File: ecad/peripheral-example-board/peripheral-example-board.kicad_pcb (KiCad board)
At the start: 2 copper layers, 105 x 70 mm, 4 parts, among them J1 Amphenol_10061913-xx0, J2 Amphenol_ACJS-MHOM, J3 Amphenol_ACJS-MHOM, J4 PJRAS2X1S01AUX

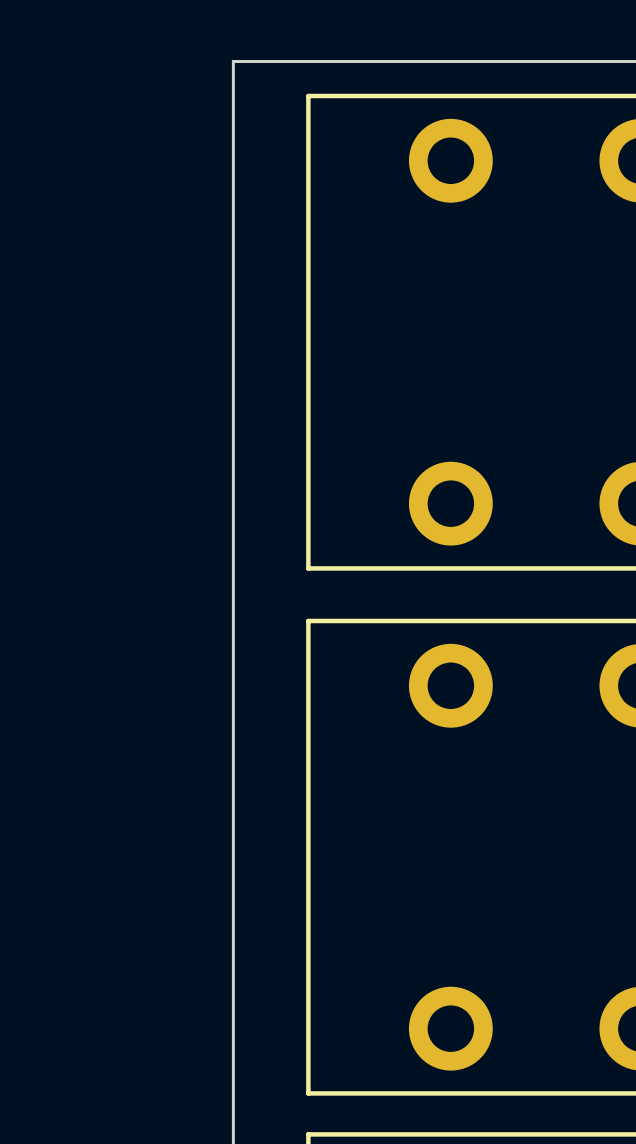
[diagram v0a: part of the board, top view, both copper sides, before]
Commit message: Good state for mechanical assembly, can bounce back to pcb review now that board outlines are close.
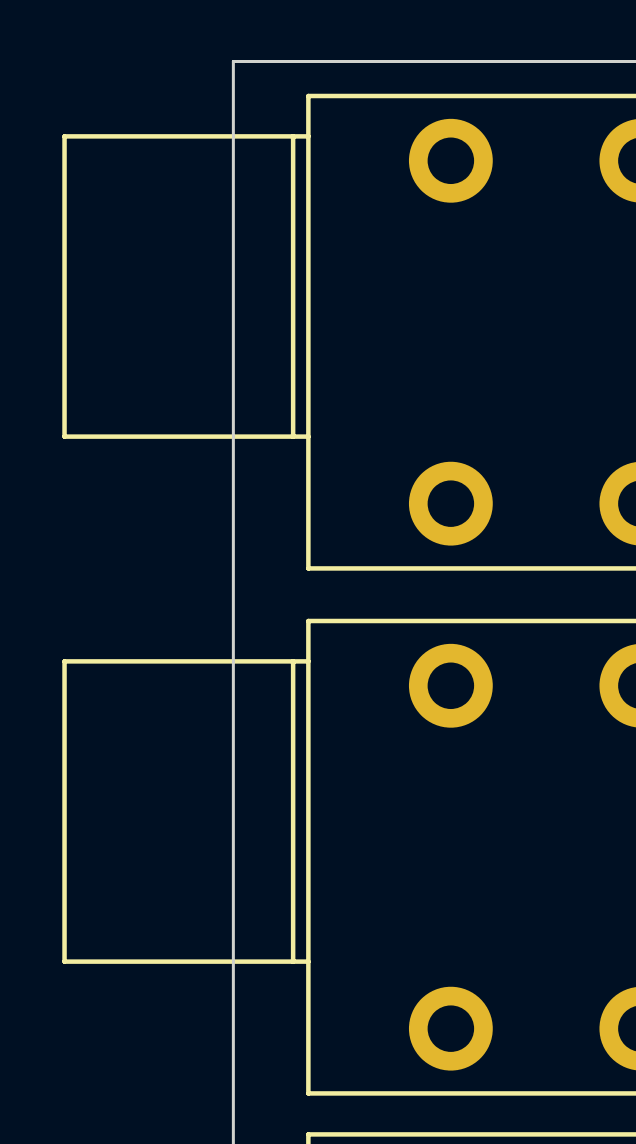
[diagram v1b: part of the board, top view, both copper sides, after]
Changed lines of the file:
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@@
     (fp_line (start 0 -9.398) (end 0 6.35)
       (stroke (width 0.15) (type solid)) (layer "F.SilkS"))
+    (fp_line (start 0 -5.0038) (end 8.128 -5.0038)
+      (stroke (width 0.15) (type solid)) (layer "F.SilkS"))
+    (fp_line (start 0 5.0038) (end 8.128 5.0038)
+      (stroke (width 0.15) (type solid)) (layer "F.SilkS"))
     (fp_line (start 0 6.35) (end -25.4 6.35)
       (stroke (width 0.15) (type solid)) (layer "F.SilkS"))
-    (fp_line (start 0 -5.0038) (end 8.128 -5.0038)
-      (stroke (width 0.15) (type solid)) (layer "Dwgs.User"))
-    (fp_line (start 0 5.0038) (end 8.128 5.0038)
-      (stroke (width 0.15) (type solid)) (layer "Dwgs.User"))
     (fp_line (start 0.508 -5.0038) (end 0.508 5.0038)
-      (stroke (width 0.15) (type solid)) (layer "Dwgs.User"))
+      (stroke (width 0.15) (type solid)) (layer "F.SilkS"))
     (fp_line (start 8.128 -5.0038) (end 8.128 5.0038)
-      (stroke (width 0.15) (type solid)) (layer "Dwgs.User"))
+      (stroke (width 0.15) (type solid)) (layer "F.SilkS"))
     (fp_line (start -25.654 -9.652) (end -25.654 6.604)
       (stroke (width 0.12) (type solid)) (layer "F.CrtYd"))
@@
     (fp_line (start 0 -9.398) (end 0 6.35)
       (stroke (width 0.15) (type solid)) (layer "F.SilkS"))
+    (fp_line (start 0 -5.0038) (end 8.128 -5.0038)
+      (stroke (width 0.15) (type solid)) (layer "F.SilkS"))
+    (fp_line (start 0 5.0038) (end 8.128 5.0038)
+      (stroke (width 0.15) (type solid)) (layer "F.SilkS"))
     (fp_line (start 0 6.35) (end -25.4 6.35)
       (stroke (width 0.15) (type solid)) (layer "F.SilkS"))
-    (fp_line (start 0 -5.0038) (end 8.128 -5.0038)
-      (stroke (width 0.15) (type solid)) (layer "Dwgs.User"))
-    (fp_line (start 0 5.0038) (end 8.128 5.0038)
-      (stroke (width 0.15) (type solid)) (layer "Dwgs.User"))
     (fp_line (start 0.508 -5.0038) (end 0.508 5.0038)
-      (stroke (width 0.15) (type solid)) (layer "Dwgs.User"))
+      (stroke (width 0.15) (type solid)) (layer "F.SilkS"))
     (fp_line (start 8.128 -5.0038) (end 8.128 5.0038)
-      (stroke (width 0.15) (type solid)) (layer "Dwgs.User"))
+      (stroke (width 0.15) (type solid)) (layer "F.SilkS"))
     (fp_line (start -25.654 -9.652) (end -25.654 6.604)
       (stroke (width 0.12) (type solid)) (layer "F.CrtYd"))
@@
     (style (thickness 0.15) (arrow_length 1.27) (text_position_mode 0) (extension_height 0.58642) (extension_offset 0.5) keep_text_aligned)
   )
+  (dimension (type aligned) (layer "Edge.Cuts")
+    (pts (xy 97.5 70.5) (xy 202.5 70.5))
+    (height -4.25)
+    (gr_text "105.0000 mm" (at 150 65.1) (layer "Edge.Cuts")
+      (effects (font (size 1 1) (thickness 0.15)))
+    )
+    (format (prefix "") (suffix "") (units 3) (units_format 1) (precision 4))
+    (style (thickness 0.1) (arrow_length 1.27) (text_position_mode 0) (extension_height 0.58642) (extension_offset 0.5) keep_text_aligned)
+  )
+  (dimension (type aligned) (layer "Edge.Cuts")
+    (pts (xy 202.5 70.5) (xy 202.5 140.5))
+    (height -5)
+    (gr_text "70.0000 mm" (at 206.35 105.5 90) (layer "Edge.Cuts")
+      (effects (font (size 1 1) (thickness 0.15)))
+    )
+    (format (prefix "") (suffix "") (units 3) (units_format 1) (precision 4))
+    (style (thickness 0.1) (arrow_length 1.27) (text_position_mode 0) (extension_height 0.58642) (extension_offset 0.5) keep_text_aligned)
+  )
+  (dimension (type aligned) (layer "Edge.Cuts")
+    (pts (xy 97.5 70.5) (xy 162.75 70.5))
+    (height -1.75)
+    (gr_text "65.2500 mm" (at 130.125 67.6) (layer "Edge.Cuts")
+      (effects (font (size 1 1) (thickness 0.15)))
+    )
+    (format (prefix "") (suffix "") (units 3) (units_format 1) (precision 4))
+    (style (thickness 0.1) (arrow_length 1.27) (text_position_mode 0) (extension_height 0.58642) (extension_offset 0.5) keep_text_aligned)
+  )
 )

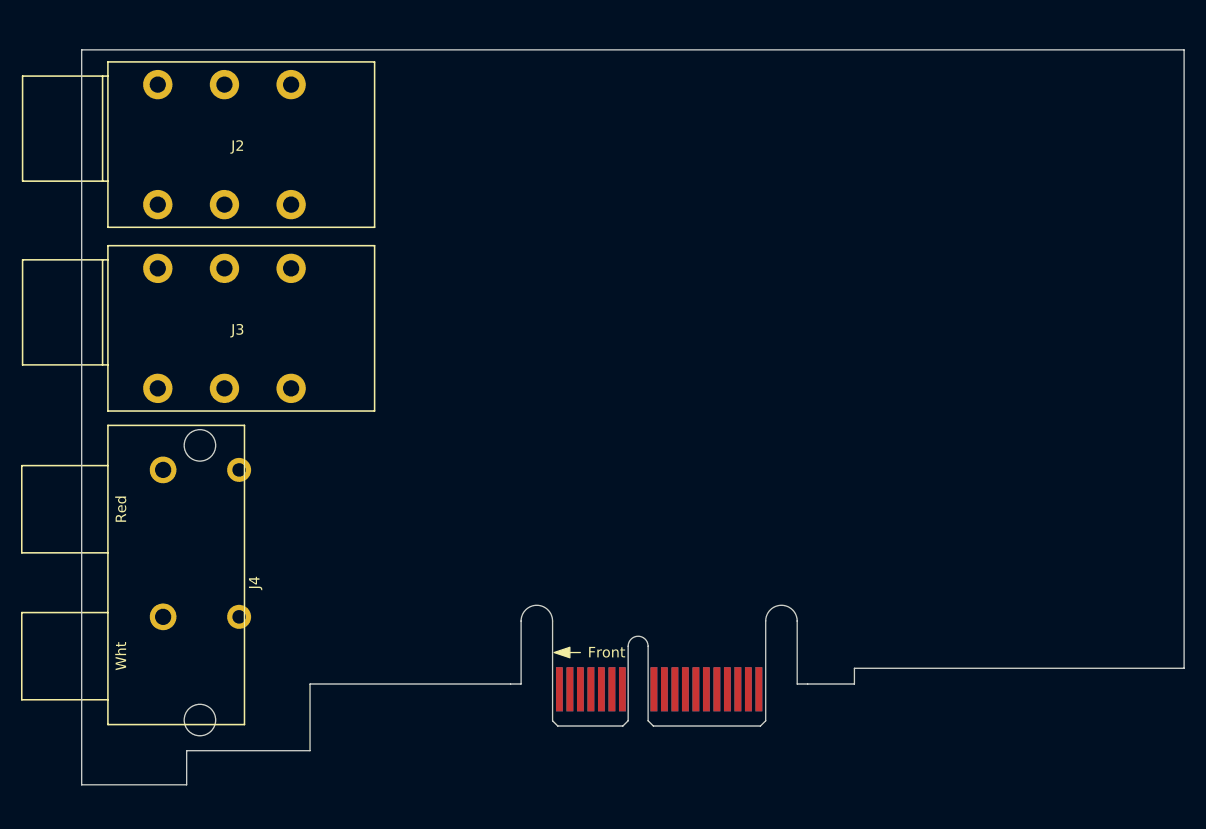
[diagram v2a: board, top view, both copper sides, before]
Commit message: Version 0.1 of the peripheral example board sent to PCB manufaturer.
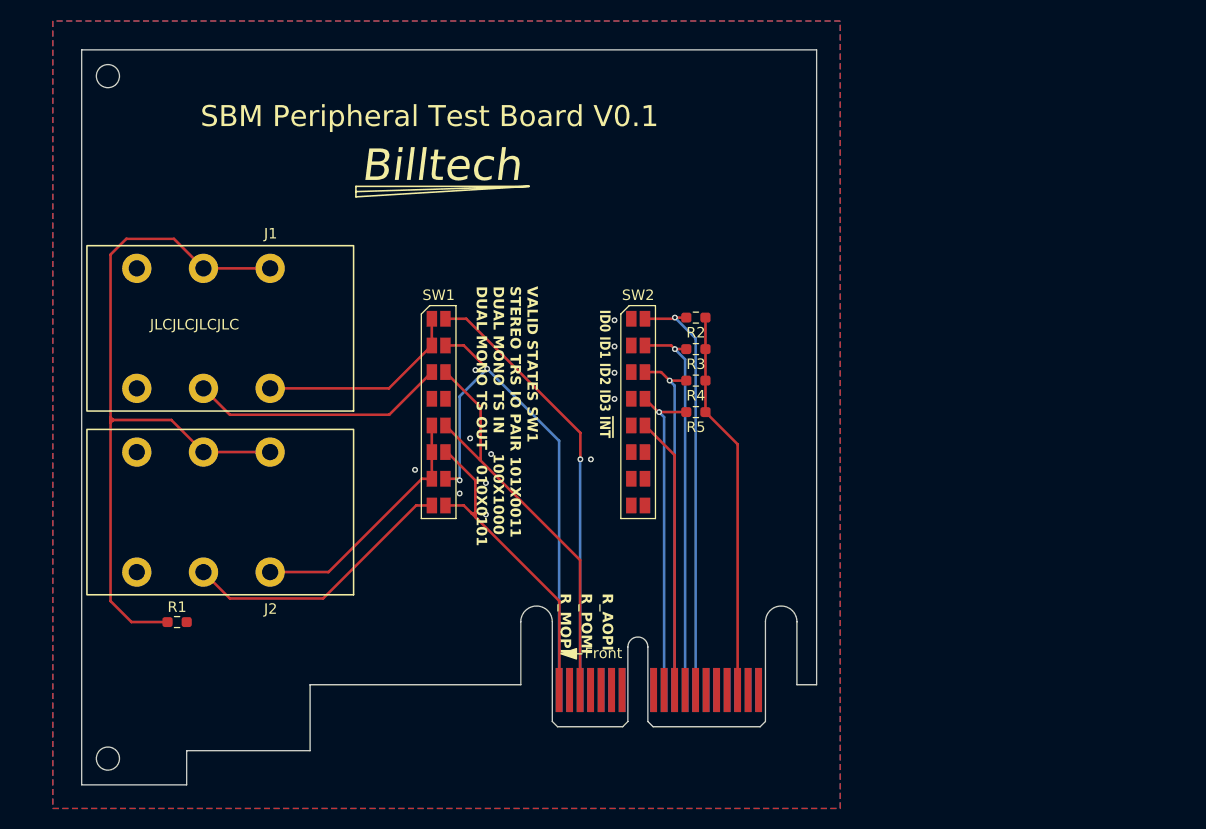
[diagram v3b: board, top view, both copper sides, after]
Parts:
- removed J3: Amphenol_ACJS-MHOM, silver-box-feetprints:ACJS-MHOM
- removed J4: PJRAS2X1S01AUX, silver-box-feetprints:PJRAS2X1S01AUX
- added LOGO: Billtech, silver-box-feetprints:Billtech, F.Cu at (132.5, 81.8)
- added P1: Amphenol_10061913-xx0, silver-box-feetprints:Card Edge board Amphenol 10061913-100PLF, F.Cu at (145.9, 135.0)
- added R1: 10k, Resistor_SMD:R_0603_1608Metric_Pad0.98x0.95mm_HandSolder, F.Cu at (106.6, 125.0)
- added R2: 10k, Resistor_SMD:R_0603_1608Metric_Pad0.98x0.95mm_HandSolder, F.Cu at (156.0, 96.0)
- added R3: 10k, Resistor_SMD:R_0603_1608Metric_Pad0.98x0.95mm_HandSolder, F.Cu at (156.0, 99.0)
- added R4: 10k, Resistor_SMD:R_0603_1608Metric_Pad0.98x0.95mm_HandSolder, F.Cu at (156.0, 102.0)
- added R5: 10k, Resistor_SMD:R_0603_1608Metric_Pad0.98x0.95mm_HandSolder, F.Cu at (156.0, 105.0)
- added REF**: MountingHole_2.2mm_M2, MountingHole:MountingHole_2.2mm_M2, F.Cu at (100.0, 73.0)
- added REF**: MountingHole_2.2mm_M2, MountingHole:MountingHole_2.2mm_M2, F.Cu at (100.0, 138.0)
- added SW1: SW_DIP_x08, silver-box-feetprints:1x8 solder bridge 1x1.5x0.3, F.Cu at (131.5, 105.0)
- added SW2: SW_DIP_x08, silver-box-feetprints:1x8 solder bridge 1x1.5x0.3, F.Cu at (150.5, 105.0)
- J1: value Amphenol_10061913-xx0 -> Amphenol_ACJS-MHOM; footprint silver-box-feetprints:Card Edge board Amphenol 10061913-100PLF -> silver-box-feetprints:ACJS-MHOM
- moved J1 65.6 mm to (98.0, 95.5), turned to 180 degrees
- moved J2 35.1 mm to (98.0, 113.0)
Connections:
- J2 pad R: unconnected-(J2-PadR) -> /R2
- J2 pad RN: unconnected-(J2-PadRN) -> Net-(J1-PadRN)
- J2 pad S: unconnected-(J2-PadS) -> GND
- J2 pad SN: unconnected-(J2-PadSN) -> GND
- J2 pad T: unconnected-(J2-PadT) -> /T2
- J2 pad TN: unconnected-(J2-PadTN) -> Net-(J1-PadRN)
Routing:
- net Net-(J1-PadRN): track 0.00 -> 73.4 mm
- net /L_MOPI: track 0.00 -> 51.4 mm, vias 0 -> 2
- net /L_POMI: track 0.00 -> 41.9 mm, vias 0 -> 1
- net /R_POMI: track 0.00 -> 40.3 mm
- net /ID0: track 0.00 -> 40.3 mm, vias 0 -> 1
- net /ID1: track 0.00 -> 37.0 mm, vias 0 -> 1
- net /+5V: track 0.00 -> 36.7 mm
- net /ID2: track 0.00 -> 33.9 mm, vias 0 -> 1
- net /R_MOPI: track 0.00 -> 31.3 mm
- net /ID3: track 0.00 -> 31.1 mm, vias 0 -> 1
- net /R2: track 0.00 -> 26.5 mm
- net /~{INT}: track 0.00 -> 26.4 mm
- net /R1: track 0.00 -> 24.5 mm
- net /T2: track 0.00 -> 24.2 mm
- net /T1: track 0.00 -> 19.6 mm
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- added copper zone on B.Cu, net GND
- added copper zone on F.Cu, net GND
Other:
- board size 105 x 70 mm -> 70 x 70 mm
- rule pad_to_mask_clearance: 0 -> 0.05
- board text added: "Billtech"
- board text added: "ID0 ID1 ID2 ID3 ~{INT}"
- board text added: "JLCJLCJLCJLC"
- board text added: "L_AOPI"
- board text added: "L_MOPI"
- board text added: "L_POMI"
- board text added: "R_AOPI"
- board text added: "R_MOPI"
- board text added: "R_POMI"
- board text added: "SBM Peripheral Test Board V0.1"
- board text added: "ToDo: - [ ] Cleanup Dimensions/Drawings - [ ] Standardize edgecut limits"
- board text added: "VALID STATES SW1 STEREO TRS IO PAIR 101X0011 DUAL MONO TS IN 100X1000 DUAL MONO TS OUT 010X0101"
